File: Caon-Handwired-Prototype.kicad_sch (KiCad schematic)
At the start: 27 parts, among them SW1 SW_PUSH_MX, SW2 SW_PUSH_MX, SW3 SW_PUSH_MX, SW4 EC11 ENCODER 1, SW5 SW_PUSH_MX, SW6 SW_PUSH_MX, SW7 SW_PUSH_MX, SW8 EC11 ENCODER 1, U1 74HC595, U2 74HC595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

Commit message: Schematic update
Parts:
- renumbered D7 to D4, D4 to D5, D5 to D6, D6 to D7
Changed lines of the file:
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@@
 		(on_board yes)
 		(dnp no)
-		(property "Reference" "D4"
+		(property "Reference" "D5"
 			(at 62.23 125.73 90)
 			(effects
@@
 			(project "Caon-Handwired-Prototype"
 				(path "/8df2f29a-df03-4271-980f-9b5acafffeb5"
-					(reference "D4")
+					(reference "D5")
 					(unit 1)
 				)
@@
 		(on_board yes)
 		(dnp no)
-		(property "Reference" "D7"
+		(property "Reference" "D4"
 			(at 113.03 105.41 0)
 			(effects
@@
 			(project "Caon-Handwired-Prototype"
 				(path "/8df2f29a-df03-4271-980f-9b5acafffeb5"
-					(reference "D7")
+					(reference "D4")
 					(unit 1)
 				)
@@
 		(on_board yes)
 		(dnp no)
-		(property "Reference" "D5"
+		(property "Reference" "D6"
 			(at 82.55 125.73 90)
 			(effects
@@
 			(project "Caon-Handwired-Prototype"
 				(path "/8df2f29a-df03-4271-980f-9b5acafffeb5"
-					(reference "D5")
+					(reference "D6")
 					(unit 1)
 				)
@@
 		(on_board yes)
 		(dnp no)
-		(property "Reference" "D6"
+		(property "Reference" "D7"
 			(at 102.87 125.73 90)
 			(effects
@@
 			(project "Caon-Handwired-Prototype"
 				(path "/8df2f29a-df03-4271-980f-9b5acafffeb5"
-					(reference "D6")
-					(unit 1)
-				)
+					(reference "D7")
+					(unit 1)
+				)

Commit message: Update
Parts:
- removed SW1, SW2, SW3, SW5, SW6, SW7: SW_PUSH_MX, Caon_Footprint:SW_PUSH_6mm, symbol Caon65:SW_PUSH_MX
- added SW1, SW2, SW3, SW5, SW6, SW7: ~, Caon_Footprint:SW_PUSH_6mm, symbol Switch:SW_Push_45deg
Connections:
- net C0: now also SW1.1, SW5.1
- net C1: now also SW2.1, SW6.1
- net C2: now also SW3.1, SW7.1
- net GND: no longer SW4.MP, SW8.MP
- net at D1.2 (A): now also SW1.2
- net at D3.2 (A): now also SW3.2
- net at D5.2 (A): now also SW5.2
- net at D6.2 (A): now also SW6.2
- net at D2.2 (A): now also SW2.2
- net at D7.2 (A): now also SW7.2
- no-connect marks 29 -> 31
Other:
- moved on the sheet: D1, D4, D8, ENC_R1, ENC_R2, ENC_R3, ENC_R4, SW4, SW8, S_D1, S_D2, S_D3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

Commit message: Update
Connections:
- net C4 is gone; now on net C2: S_D4.1 (K)
- net C0: now also S_D3.1 (K)
- net C2: no longer S_D3.1 (K)

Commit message: Schematic Update
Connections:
- net GND: no longer ENC_R2.1, SW4.A, U3.11 (P1.04-LF)
- new net ENC1_A: ENC_R2.1, SW4.A, U3.11 (P1.04-LF)
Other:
- moved on the sheet: ENC_R1, ENC_R2
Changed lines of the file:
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@@
 	)
 	(junction
-		(at 137.16 125.73)
+		(at 138.43 125.73)
 		(diameter 0)
 		(color 0 0 0 0)
@@
 	)
 	(junction
-		(at 127 113.03)
+		(at 128.27 113.03)
 		(diameter 0)
 		(color 0 0 0 0)
@@
 	)
 	(junction
-		(at 123.19 118.11)
-		(diameter 0)
-		(color 0 0 0 0)
-	)
-	(junction
 		(at 138.43 157.48)
 		(diameter 0)
@@
 	)
 	(junction
-		(at 125.73 118.11)
+		(at 127 118.11)
 		(diameter 0)
 		(color 0 0 0 0)
@@
 	(wire
 		(pts
-			(xy 127 113.03) (xy 121.92 113.03)
-		)
-		(stroke
-			(width 0)
-			(type default)
-		)
-	)
-	(wire
-		(pts
-			(xy 127 125.73) (xy 127 113.03)
+			(xy 128.27 125.73) (xy 128.27 113.03)
 		)
 		(stroke
@@
 	(wire
 		(pts
-			(xy 127 113.03) (xy 127 111.76)
-		)
-		(stroke
-			(width 0)
-			(type default)
-		)
-	)
-	(wire
-		(pts
 			(xy 74.93 118.11) (xy 88.9 118.11)
 		)
@@
 	(wire
 		(pts
-			(xy 125.73 118.11) (xy 125.73 116.84)
-		)
-		(stroke
-			(width 0)
-			(type default)
-		)
-	)
-	(wire
-		(pts
 			(xy 137.16 165.1) (xy 138.43 165.1)
 		)
@@
 	(wire
 		(pts
-			(xy 127 111.76) (xy 128.27 111.76)
+			(xy 128.27 113.03) (xy 129.54 113.03)
 		)
 		(stroke
@@
 	(wire
 		(pts
-			(xy 123.19 118.11) (xy 123.19 115.57)
+			(xy 123.19 115.57) (xy 123.19 119.38)
 		)
 		(stroke
@@
 	(wire
 		(pts
-			(xy 128.27 125.73) (xy 127 125.73)
+			(xy 129.54 125.73) (xy 128.27 125.73)
 		)
 		(stroke
@@
 	(wire
 		(pts
-			(xy 125.73 133.35) (xy 125.73 118.11)
+			(xy 127 133.35) (xy 127 118.11)
 		)
 		(stroke
@@
 	(wire
 		(pts
-			(xy 137.16 133.35) (xy 137.16 125.73)
+			(xy 138.43 133.35) (xy 138.43 125.73)
 		)
 		(stroke
@@
 	(wire
 		(pts
-			(xy 135.89 125.73) (xy 137.16 125.73)
+			(xy 137.16 125.73) (xy 138.43 125.73)
 		)
 		(stroke
@@
 	(wire
 		(pts
-			(xy 125.73 118.11) (xy 123.19 118.11)
+			(xy 74.93 134.62) (xy 74.93 135.89)
 		)
 		(stroke
@@
 	(wire
 		(pts
-			(xy 74.93 134.62) (xy 74.93 135.89)
+			(xy 58.42 54.61) (xy 58.42 57.15)
 		)
 		(stroke
@@
 	(wire
 		(pts
-			(xy 58.42 54.61) (xy 58.42 57.15)
+			(xy 62.23 116.84) (xy 62.23 118.11)
 		)
 		(stroke
@@
 	(wire
 		(pts
-			(xy 62.23 116.84) (xy 62.23 118.11)
+			(xy 128.27 157.48) (xy 128.27 143.51)
 		)
 		(stroke
@@
 	(wire
 		(pts
-			(xy 128.27 157.48) (xy 128.27 143.51)
+			(xy 137.16 133.35) (xy 138.43 133.35)
 		)
 		(stroke
@@
 	(wire
 		(pts
-			(xy 135.89 133.35) (xy 137.16 133.35)
+			(xy 127 118.11) (xy 129.54 118.11)
 		)
 		(stroke
@@
 	(wire
 		(pts
-			(xy 125.73 116.84) (xy 128.27 116.84)
+			(xy 83.82 104.14) (xy 82.55 104.14)
 		)
 		(stroke
@@
 	(wire
 		(pts
-			(xy 83.82 104.14) (xy 82.55 104.14)
+			(xy 100.33 43.18) (xy 100.33 57.15)
 		)
 		(stroke
@@
 	(wire
 		(pts
-			(xy 100.33 43.18) (xy 100.33 57.15)
+			(xy 143.51 81.28) (xy 143.51 80.01)
 		)
 		(stroke
@@
 	(wire
 		(pts
-			(xy 143.51 81.28) (xy 143.51 80.01)
+			(xy 121.92 113.03) (xy 128.27 113.03)
 		)
 		(stroke
@@
 	(wire
 		(pts
-			(xy 128.27 133.35) (xy 125.73 133.35)
+			(xy 129.54 133.35) (xy 127 133.35)
 		)
 		(stroke
@@
 	(wire
 		(pts
-			(xy 123.19 118.11) (xy 121.92 118.11)
+			(xy 121.92 118.11) (xy 127 118.11)
 		)
 		(stroke
@@
 	(wire
 		(pts
-			(xy 137.16 125.73) (xy 142.24 125.73)
+			(xy 138.43 125.73) (xy 143.51 125.73)
 		)
 		(stroke
@@
 	(global_label "ENC1_A"
 		(shape output)
-		(at 128.27 116.84 0)
+		(at 129.54 118.11 0)
 		(fields_autoplaced yes)
 		(effects
@@
 		)
 		(property "Intersheetrefs" "${INTERSHEET_REFS}"
-			(at 138.2704 116.84 0)
+			(at 139.5404 118.11 0)
 			(effects
 				(font
@@
 	(global_label "ENC1_B"
 		(shape output)
-		(at 128.27 111.76 0)
+		(at 129.54 113.03 0)
 		(fields_autoplaced yes)
 		(effects
@@
 		)
 		(property "Intersheetrefs" "${INTERSHEET_REFS}"
-			(at 138.4518 111.76 0)
+			(at 139.7218 113.03 0)
 			(effects
 				(font
@@
 	(symbol
 		(lib_id "power:GND")
-		(at 123.19 118.11 0)
+		(at 123.19 119.38 0)
 		(unit 1)
 		(exclude_from_sim no)
@@
 		(dnp no)
 		(property "Reference" "#PWR08"
-			(at 123.19 124.46 0)
+			(at 123.19 125.73 0)
 			(effects
 				(font
@@
 		)
 		(property "Value" "GND"
-			(at 123.19 121.92 0)
+			(at 123.19 123.19 0)
 			(effects
 				(font
@@
 		)
 		(property "Footprint" ""
-			(at 123.19 118.11 0)
+			(at 123.19 119.38 0)
 			(effects
 				(font
@@
 		)
 		(property "Datasheet" ""
-			(at 123.19 118.11 0)
+			(at 123.19 119.38 0)
 			(effects
 				(font
@@
 		)
 		(property "Description" "Power symbol creates a global label with name \"GND\" , ground"
-			(at 123.19 118.11 0)
+			(at 123.19 119.38 0)
 			(effects
 				(font
@@
 	(symbol
 		(lib_id "Device:R")
-		(at 132.08 125.73 90)
+		(at 133.35 125.73 90)
 		(unit 1)
 		(exclude_from_sim no)
@@
 		(dnp no)
 		(property "Reference" "ENC_R1"
-			(at 132.08 120.65 90)
+			(at 133.35 120.65 90)
 			(effects
 				(font
@@
 		)
 		(property "Value" "10k"
-			(at 132.08 123.19 90)
+			(at 133.35 123.19 90)
 			(effects
 				(font
@@
 		)
 		(property "Footprint" "Resistor_THT:R_Axial_DIN0204_L3.6mm_D1.6mm_P2.54mm_Vertical"
-			(at 132.08 127.508 90)
+			(at 133.35 127.508 90)
 			(effects
 				(font
@@
 		)
 		(property "Datasheet" "~"
-			(at 132.08 125.73 0)
+			(at 133.35 125.73 0)
 			(effects
 				(font
@@
 		)
 		(property "Description" "Resistor"
-			(at 132.08 125.73 0)
+			(at 133.35 125.73 0)
 			(effects
 				(font
@@
 	(symbol
 		(lib_id "Device:R")
-		(at 132.08 133.35 90)
+		(at 133.35 133.35 90)
 		(unit 1)
 		(exclude_from_sim no)
@@
 		(dnp no)
 		(property "Reference" "ENC_R2"
-			(at 132.08 128.27 90)
+			(at 133.35 128.27 90)
 			(effects
 				(font
@@
 		)
 		(property "Value" "10k"
-			(at 132.08 130.81 90)
+			(at 133.35 130.81 90)
 			(effects
 				(font
@@
 		)
 		(property "Footprint" "Resistor_THT:R_Axial_DIN0204_L3.6mm_D1.6mm_P2.54mm_Vertical"
-			(at 132.08 135.128 90)
+			(at 133.35 135.128 90)
 			(effects
 				(font
@@
 		)
 		(property "Datasheet" "~"
-			(at 132.08 133.35 0)
+			(at 133.35 133.35 0)
 			(effects
 				(font
@@
 		)
 		(property "Description" "Resistor"
-			(at 132.08 133.35 0)
+			(at 133.35 133.35 0)
 			(effects
 				(font
@@
 	(symbol
 		(lib_id "power:VCC")
-		(at 142.24 125.73 0)
+		(at 143.51 125.73 0)
 		(unit 1)
 		(exclude_from_sim no)
@@
 		(dnp no)
 		(property "Reference" "#PWR09"
-			(at 142.24 129.54 0)
+			(at 143.51 129.54 0)
 			(effects
 				(font
@@
 		)
 		(property "Value" "+3V3"
-			(at 142.24 120.65 0)
+			(at 143.51 120.65 0)
 			(effects
 				(font
@@
 		)
 		(property "Footprint" ""
-			(at 142.24 125.73 0)
+			(at 143.51 125.73 0)
 			(effects
 				(font
@@
 		)
 		(property "Datasheet" ""
-			(at 142.24 125.73 0)
+			(at 143.51 125.73 0)
 			(effects
 				(font
@@
 		)
 		(property "Description" "Power symbol creates a global label with name \"VCC\""
-			(at 142.24 125.73 0)
+			(at 143.51 125.73 0)
 			(effects
 				(font

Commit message: Schematic update
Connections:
- net Row 0 is gone; now on net R0: U3.17 (P0.31-LF)
- net Row 1 is gone; now on net R1: U3.18 (P0.29-LF)
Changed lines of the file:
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@@
 		)
 	)
-	(global_label "Row 0"
+	(global_label "R0"
 		(shape input)
 		(at 97.79 59.69 0)
@@
 		)
 		(property "Intersheetrefs" "${INTERSHEET_REFS}"
-			(at 106.7018 59.69 0)
+			(at 103.2547 59.69 0)
 			(effects
 				(font
@@
 		)
 	)
-	(global_label "Row 1"
+	(global_label "R1"
 		(shape input)
 		(at 97.79 62.23 0)
@@
 		)
 		(property "Intersheetrefs" "${INTERSHEET_REFS}"
-			(at 106.7018 62.23 0)
-			(effects
-				(font
+			(at 103.2547 62.23 0)
+			(effects
+				(font

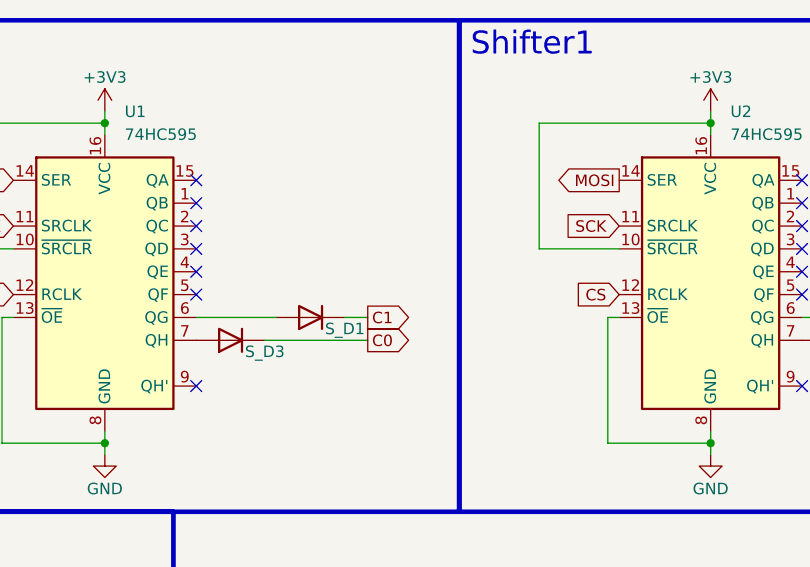
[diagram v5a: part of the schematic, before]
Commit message: fix: 2nd 595 as 2nd Device
instead of daisy chained
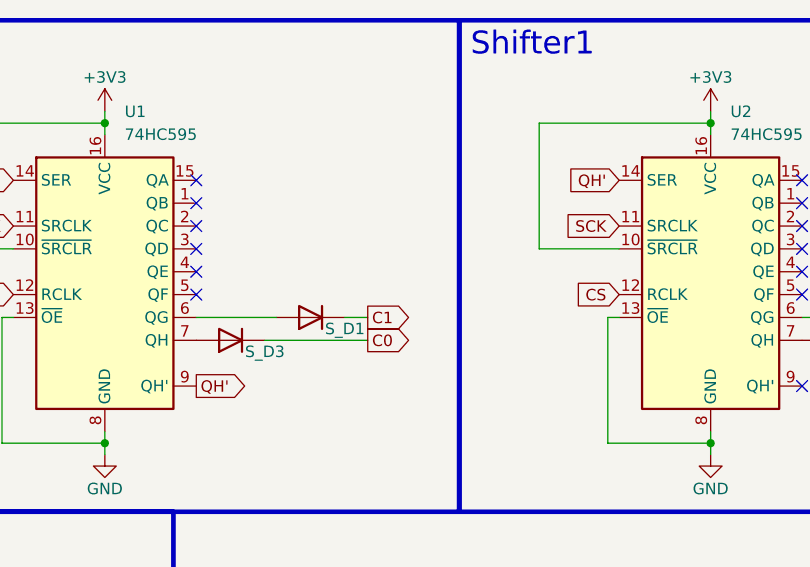
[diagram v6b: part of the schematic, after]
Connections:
- net MOSI: no longer U2.14 (SER)
- net QH': now reaches U1.9 (QH')
- net QH': now also U2.14 (SER)
- no-connect marks 31 -> 30
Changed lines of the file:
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@@
-	)
-	(no_connect
-		(at 153.67 73.66)
 	)
 	(no_connect
@@
 			(width 0)
 			(type default)
-		)
-	)
-	(global_label "MOSI"
-		(shape output)
-		(at 200.66 50.8 180)
-		(fields_autoplaced yes)
-		(effects
-			(font
-				(size 1.27 1.27)
-			)
-			(justify right)
-		)
-		(property "Intersheetrefs" "${INTERSHEET_REFS}"
-			(at 193.0786 50.8 0)
-			(effects
-				(font
-					(size 1.27 1.27)
-				)
-				(justify right)
-				(hide yes)
-			)
 		)
 	)
@@
 		)
 	)
+	(global_label "QH'"
+		(shape output)
+		(at 153.67 73.66 0)
+		(fields_autoplaced yes)
+		(effects
+			(font
+				(size 1.27 1.27)
+			)
+			(justify left)
+		)
+		(property "Intersheetrefs" "${INTERSHEET_REFS}"
+			(at 159.921 73.66 0)
+			(effects
+				(font
+					(size 1.27 1.27)
+				)
+				(justify left)
+				(hide yes)
+			)
+		)
+	)
 	(global_label "C1"
 		(shape input)
@@
 				(hide yes)
 			)
+		)
+	)
+	(global_label "QH'"
+		(shape input)
+		(at 200.66 50.8 180)
+		(fields_autoplaced yes)
+		(effects
+			(font
+				(size 1.27 1.27)
+			)
+			(justify right)
+		)
+		(property "Intersheetrefs" "${INTERSHEET_REFS}"
+			(at 194.409 50.8 0)
+			(effects
+				(font
+					(size 1.27 1.27)
+				)
+				(justify right)
+				(hide yes)
+			)

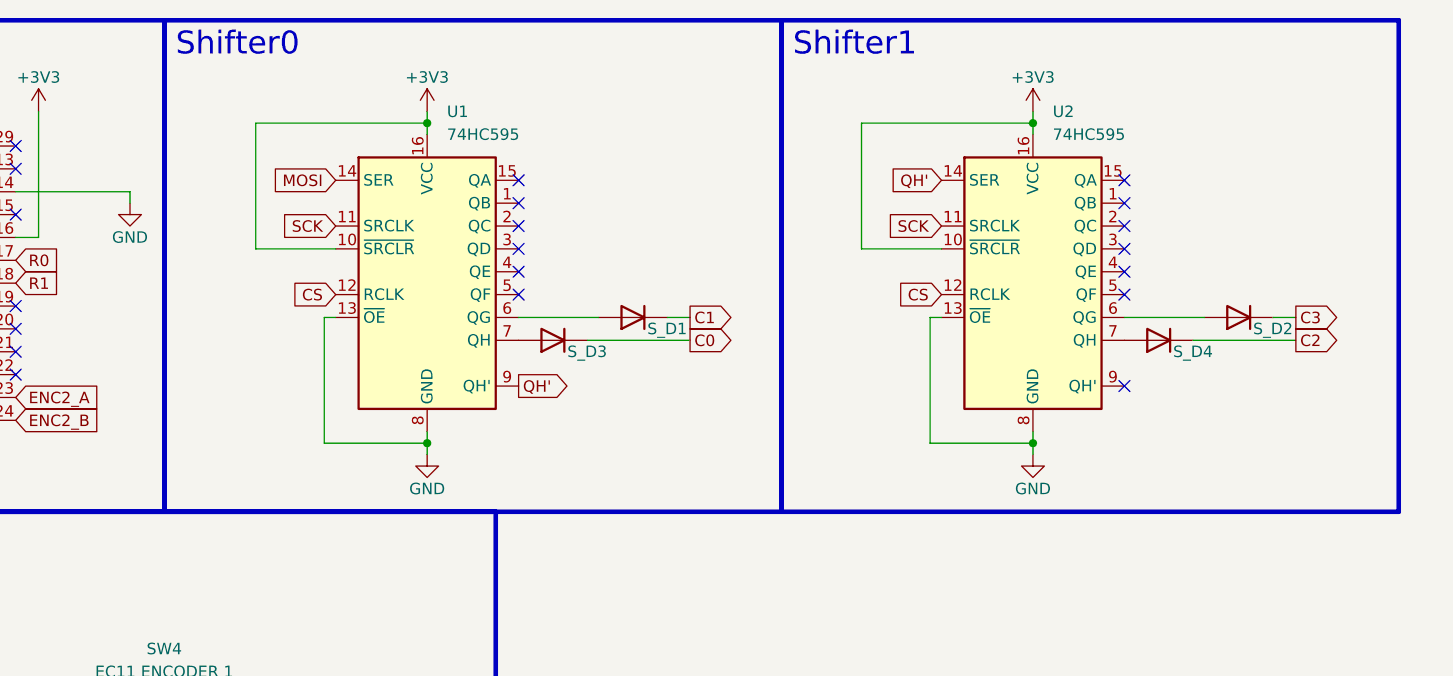
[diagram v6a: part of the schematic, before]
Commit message: Added pin description for firmware development
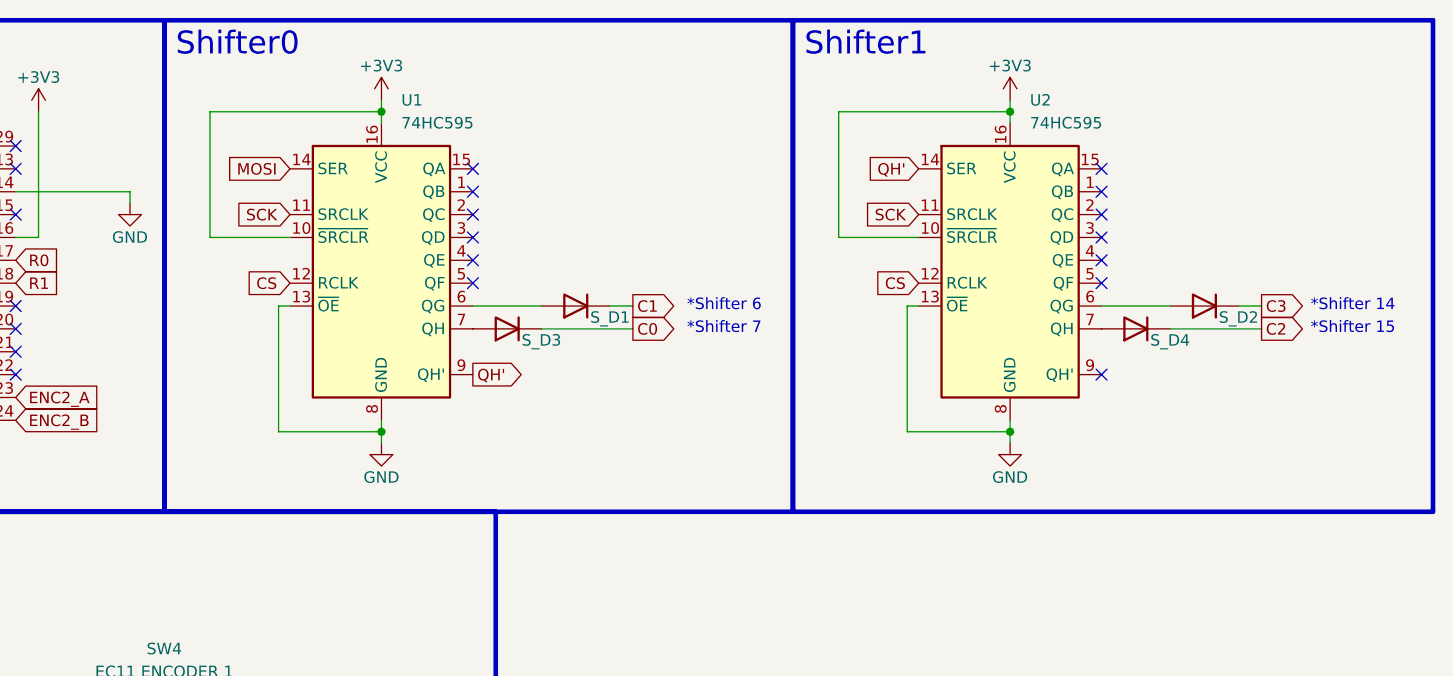
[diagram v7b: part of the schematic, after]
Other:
- note added: "*Shifter 14"
- note added: "*Shifter 15"
- note added: "*Shifter 6"
- note added: "*Shifter 7"
- moved on the sheet: S_D1, S_D2, S_D3, S_D4, U1, U2
